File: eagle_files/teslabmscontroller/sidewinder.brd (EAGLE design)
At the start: 101.6 x 73.2 mm, 41 parts, among them J1 TERMINAL12, J2 TERMINAL12, Q1 2N3704, Q2 2N3906, T1 V_REG_317SINK, U1 G3VM41, U2 G3VM41, U3 G3VM41, U4 SN65HVD230, U5 SP720APP, U6 SP720APP

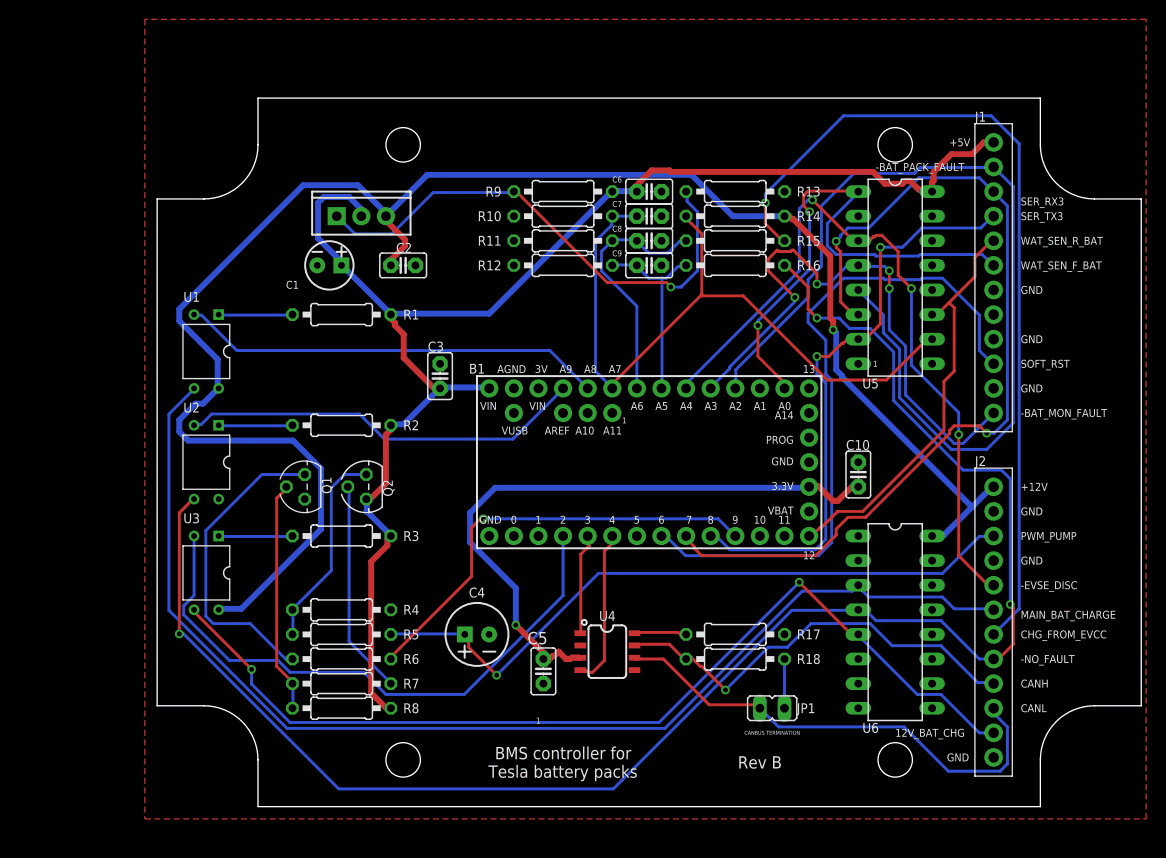
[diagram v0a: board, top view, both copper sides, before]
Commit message: fixed RUN
RUN signal was absent from connector
flipped whole board so silk alligns with OLED
fixed routing issu of can chip
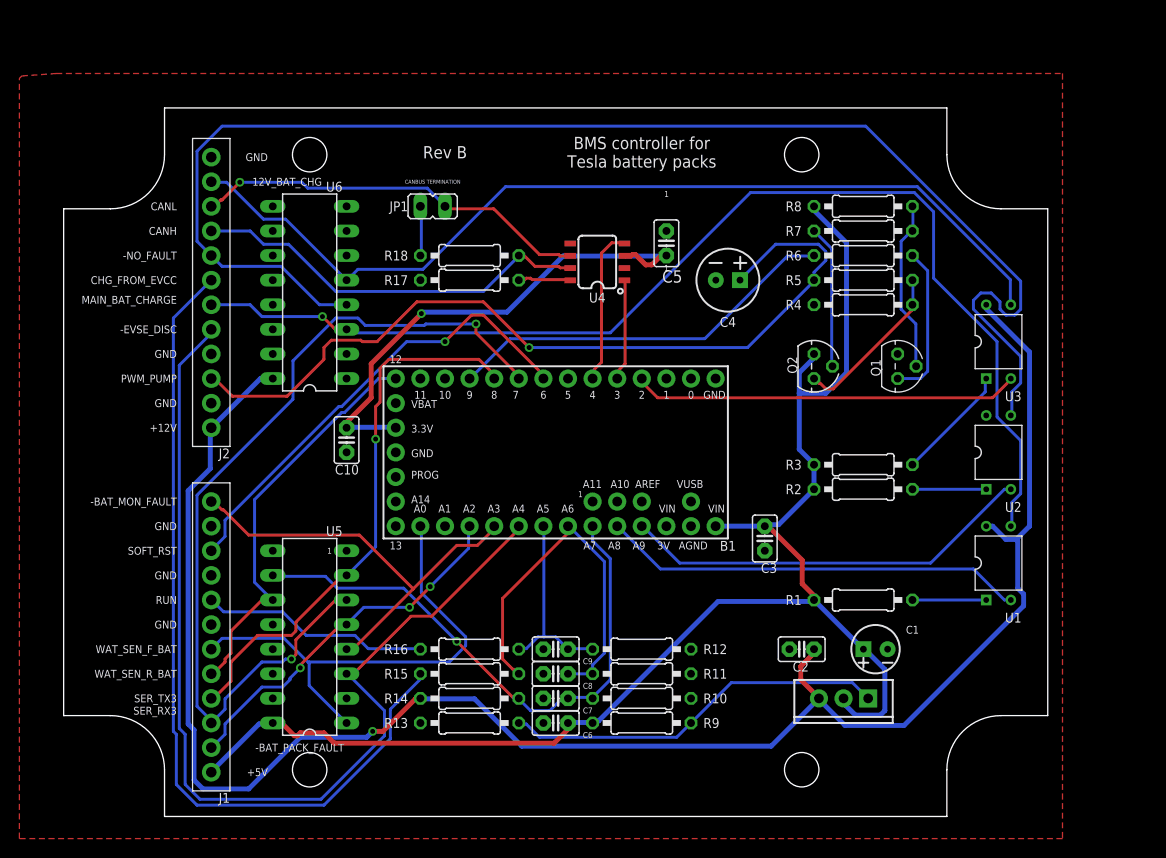
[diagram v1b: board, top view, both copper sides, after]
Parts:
- moved J2 94.3 mm to (3.05, 55.6), turned to 180 degrees
- moved J1 91.6 mm to (3.05, 20.1), turned to 180 degrees
- moved U3 85.2 mm to (86.9, 48.0), turned to 90 degrees
- moved U1 84.7 mm to (86.9, 25.1), turned to 90 degrees
- moved U2 81.8 mm to (86.9, 36.6), turned to 90 degrees
- moved R8 74.7 mm to (72.9, 62.0), turned to 180 degrees
- moved U5 72.3 mm to (15.7, 16.3), turned to 90 degrees
- moved R7 71.3 mm to (72.9, 59.4), turned to 180 degrees
- moved T1 70.4 mm to (70.9, 11.2), turned to 180 degrees
- moved C1 68.9 mm to (74.2, 16.3), turned to 180 degrees
- moved U6 68.2 mm to (15.7, 51.8), turned to 90 degrees
- moved R6 68.1 mm to (72.9, 56.9), turned to 0 degrees
- moved R5 65.1 mm to (72.9, 54.4), turned to 180 degrees
- moved JP1 62.6 mm to (28.4, 62.0), turned to 90 degrees
- moved Q1 62.5 mm to (76.5, 45.5), turned to 270 degrees
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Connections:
- net N$4 renamed PWM_PUMP
- new net RUN: J1.J8, R16.2
- net -NO_FAULT: no longer R16.2
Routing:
- net -BAT_PACK_FAULT: track 97.2 -> 38.4 mm, vias 0 -> 3
- net -EVSE_DISC: track 75.5 -> 104.9 mm, vias 3 -> 0
- net -NO_FAULT: track 171.8 -> 144.3 mm, vias 3 -> 0
- net RUN: track 0.00 -> 23.7 mm
- net SOFT_RST: track 70.2 -> 48.4 mm, vias 0 -> 1
- net -12V_BAT_CHG: track 61.5 -> 40.1 mm
- net PWM_PUMP: track 70.5 -> 86.9 mm
- net N$5: track 32.2 -> 16.0 mm
- net -BAT_MON_FAULT: track 60.2 -> 45.3 mm, vias 4 -> 0
- net 12VBAT_MON: track 73.4 -> 58.8 mm, vias 0 -> 1
- net N$15: track 53.3 -> 39.7 mm, vias 1 -> 0
- net CHARGING: track 26.1 -> 38.8 mm
- net +3V3: track 65.4 -> 53.2 mm
- net +12V: track 179.3 -> 190.3 mm
- net CANL: track 50.0 -> 41.3 mm, vias 0 -> 1
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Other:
- board text added: "RUN"

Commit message: bug fixes
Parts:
- added R19: 1k, rcl:0207/10
- moved R17 2.54 mm to (32.3, 51.8)
- moved R18 2.54 mm to (32.3, 54.4)
- moved C10 1.78 mm to (21.3, 37.8)
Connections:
- net -NO_FAULT: now also R19.1
- net CHARGING_FROM_EVCC: now also U6.12
- net RUN: now also R19.2, U6.15
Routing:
- net RUN: track 23.7 -> 75.8 mm, vias 0 -> 3
- net -NO_FAULT: track 144.3 -> 107.4 mm
- net CHARGING_FROM_EVCC: track 87.7 -> 53.7 mm, vias 0 -> 2
- net MAIN_BAT_CHARGE: track 119.3 -> 150.1 mm, vias 1 -> 0
- net SERIAL_TX3: track 57.1 -> 83.9 mm, vias 1 -> 3
- net +12V: track 190.3 -> 170.5 mm, vias 1 -> 3
- net -BAT_PACK_FAULT: track 38.4 -> 57.2 mm, vias 3 -> 1
- net PWM_PUMP: track 86.9 -> 73.0 mm, vias 1 -> 0
- net WAT_SEN_F_BAT: track 50.7 -> 41.1 mm
- net -EVSE_DISC: track 104.9 -> 96.4 mm, vias 0 -> 2
- net SOFT_RST: track 48.4 -> 54.2 mm
- net -BAT_MON_FAULT: track 45.3 -> 49.5 mm, vias 0 -> 1
- net 12VBAT_MON: track 58.8 -> 62.6 mm, vias 1 -> 0
- net N$13: track 5.16 -> 8.61 mm
- net CANH: track 41.8 -> 44.2 mm, vias 0 -> 1
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
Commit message: run and charging to zener
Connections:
- removed net N$2: B1.19, C9.1, R12.2, R16.1
- new net RUN_SW: J1.J8, R16.2
- net CHARGING: now also U5.9
- net RUN: now also B1.19, C9.1, R12.2, R16.1, U5.12; no longer J1.J8, R16.2
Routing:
- net RUN: track 75.8 -> 119.8 mm, vias 3 -> 0
- net CHARGING_FROM_EVCC: track 53.7 -> 93.1 mm, vias 2 -> 0
- net RUN_SW: track 0.00 -> 25.6 mm
- net CHARGING: track 38.8 -> 62.1 mm, vias 0 -> 2
- net WAT_SEN_R_BAT: track 40.1 -> 62.5 mm, vias 2 -> 0
- net MAIN_BAT_CHARGE: track 150.1 -> 127.9 mm, vias 0 -> 1
- net N$2: track 20.2 -> 0.00 mm
- net -BAT_PACK_FAULT: track 57.2 -> 40.3 mm, vias 1 -> 3
- net -EVSE_DISC: track 96.4 -> 112.7 mm, vias 2 -> 1
- net SERIAL_TX3: track 83.9 -> 68.2 mm, vias 3 -> 4
- net WAT_SEN_F_BAT: track 41.1 -> 52.4 mm
- net CANL: track 41.7 -> 50.2 mm
- net PWM_PUMP: track 73.0 -> 81.1 mm, vias 0 -> 2
- net +5V: track 152.7 -> 146.5 mm
- net N$13: track 8.61 -> 11.9 mm
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
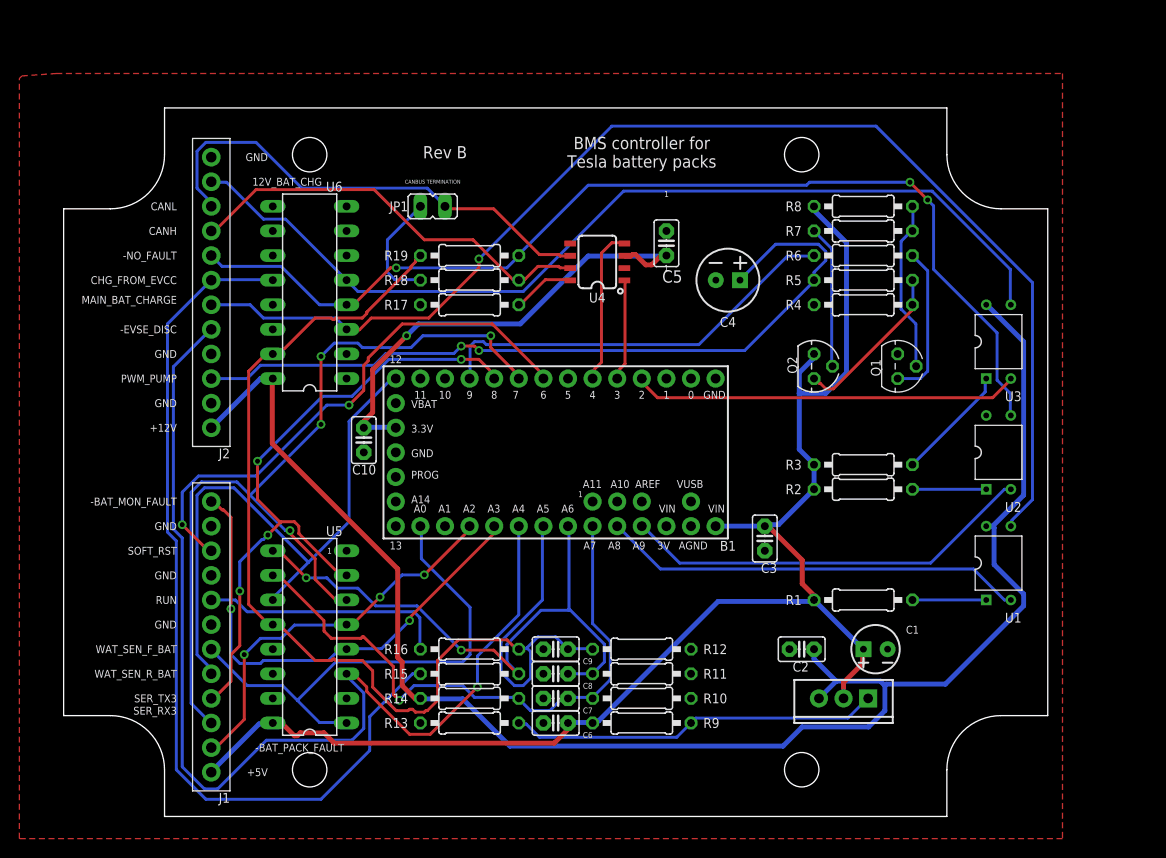
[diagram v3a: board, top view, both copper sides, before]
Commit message: adjusted 12Vto5V deviders
changed 2 resistors from 10k to 15k after we fried a board...
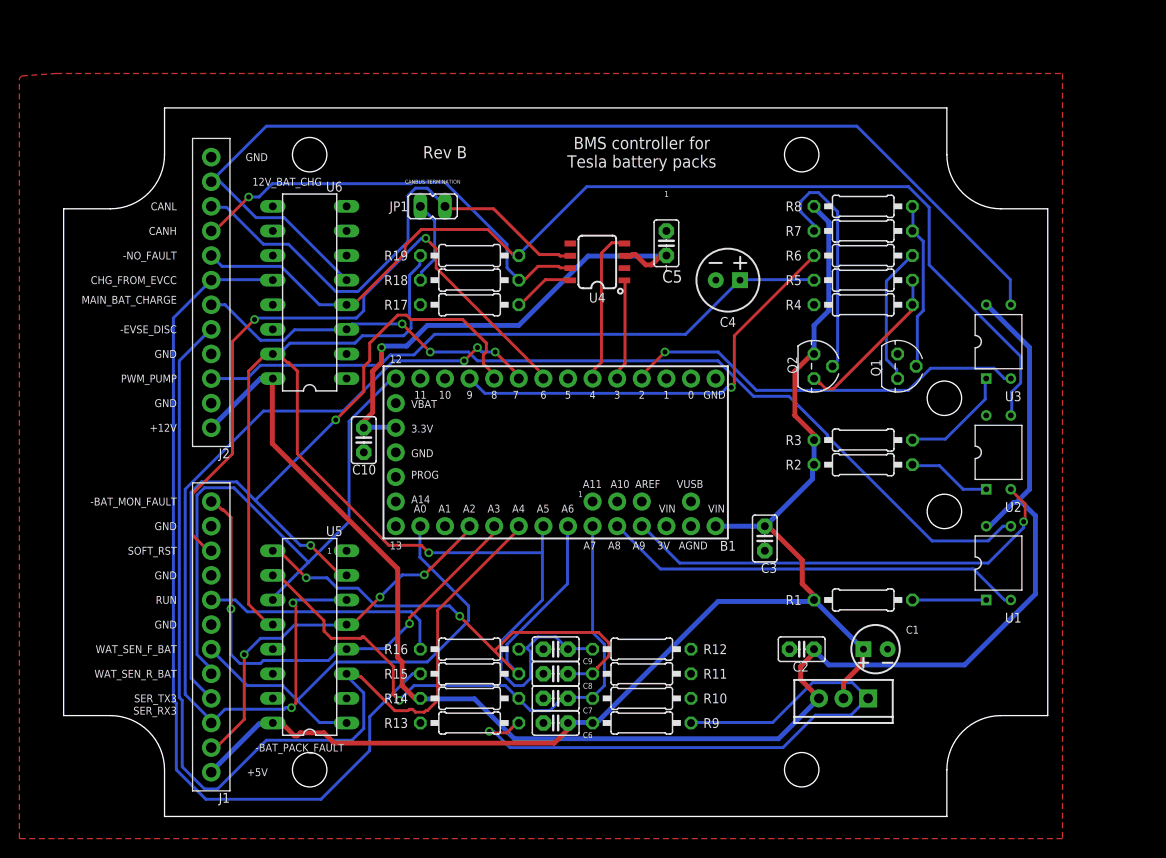
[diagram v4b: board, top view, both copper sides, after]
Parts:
- R15, R16: value 10k -> 15k
- moved R2 2.54 mm to (72.9, 35.3)
- moved R3 2.54 mm to (72.9, 37.8)
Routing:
- net MAIN_BAT_CHARGE: track 127.9 -> 94.8 mm, vias 1 -> 2
- net N$15: track 38.4 -> 66.2 mm, vias 0 -> 1
- net PWM_PUMP: track 81.1 -> 66.5 mm, vias 2 -> 0
- net SERIAL_TX3: track 68.2 -> 82.5 mm, vias 4 -> 2
- net 12V_BAT_CHG: track 98.5 -> 112.6 mm
- net SOFT_RST: track 56.2 -> 69.1 mm
- net N$7: track 14.8 -> 24.8 mm
- net RUN: track 119.8 -> 128.4 mm, vias 0 -> 1
- net +5V: track 146.5 -> 138.7 mm
- net CHARGING: track 62.1 -> 68.5 mm
- net +12V: track 168.1 -> 163.3 mm
- net N$1: track 42.8 -> 47.2 mm, vias 0 -> 1
- net -EVSE_DISC: track 112.7 -> 108.5 mm, vias 1 -> 0
- net SERIAL_RX3: track 89.4 -> 93.0 mm, vias 4 -> 5
- net N$13: track 11.9 -> 8.86 mm
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
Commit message: added EVCC_config.txt
added the config of the EVCC controller
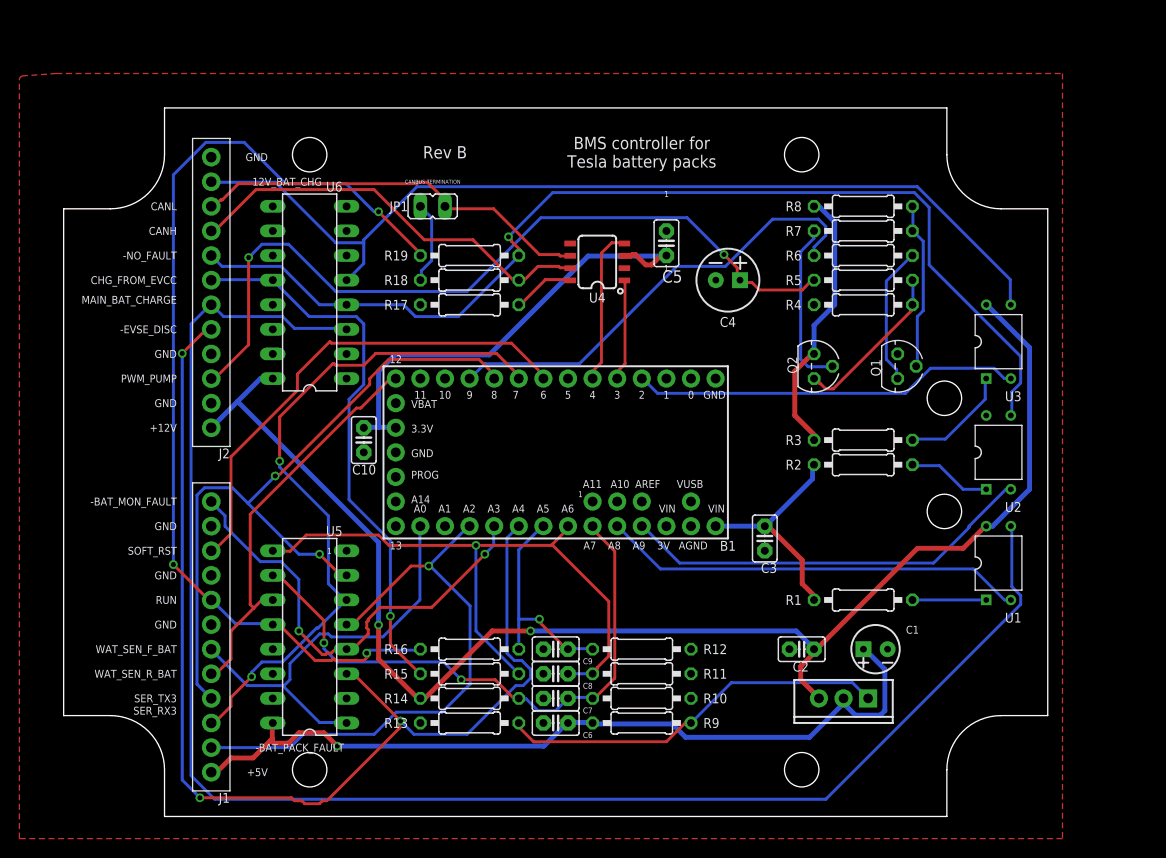
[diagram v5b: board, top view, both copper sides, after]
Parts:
- R15, R16: value 15k -> 20k
- R19: value 1k -> 20k
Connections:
- net +3V3: now also R1.1, R2.1, R3.1
- net +5V: now also R19.2; no longer R1.1, R2.1, R3.1
- net RUN: no longer R19.2, U5.12, U6.15
- net RUN_SW: now also U5.12
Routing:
- net RUN: track 128.4 -> 23.0 mm
- net RUN_SW: track 25.4 -> 102.6 mm, vias 0 -> 3
- net MAIN_BAT_CHARGE: track 94.8 -> 168.1 mm, vias 2 -> 0
- net CHARGING_FROM_EVCC: track 92.6 -> 57.5 mm, vias 0 -> 1
- net N$15: track 66.2 -> 40.3 mm, vias 1 -> 0
- net SERIAL_RX3: track 93.0 -> 70.7 mm, vias 5 -> 2
- net WAT_SEN_R_BAT: track 62.5 -> 41.9 mm
- net -BAT_PACK_FAULT: track 40.3 -> 60.4 mm, vias 3 -> 1
- net SOFT_RST: track 69.1 -> 50.7 mm, vias 2 -> 0
- net PWM_PUMP: track 66.5 -> 82.6 mm, vias 0 -> 2
- net +12V: track 163.3 -> 147.9 mm, vias 0 -> 2
- net 12V_BAT_CHG: track 112.6 -> 98.9 mm
- net CANL: track 50.9 -> 41.7 mm
- net -EVSE_DISC: track 108.5 -> 117.3 mm, vias 0 -> 3
- net SERIAL_TX3: track 82.5 -> 74.1 mm
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
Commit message: updated BMS board
fixed can bus chip and changed 5v regulator to a switching to avoid heat.
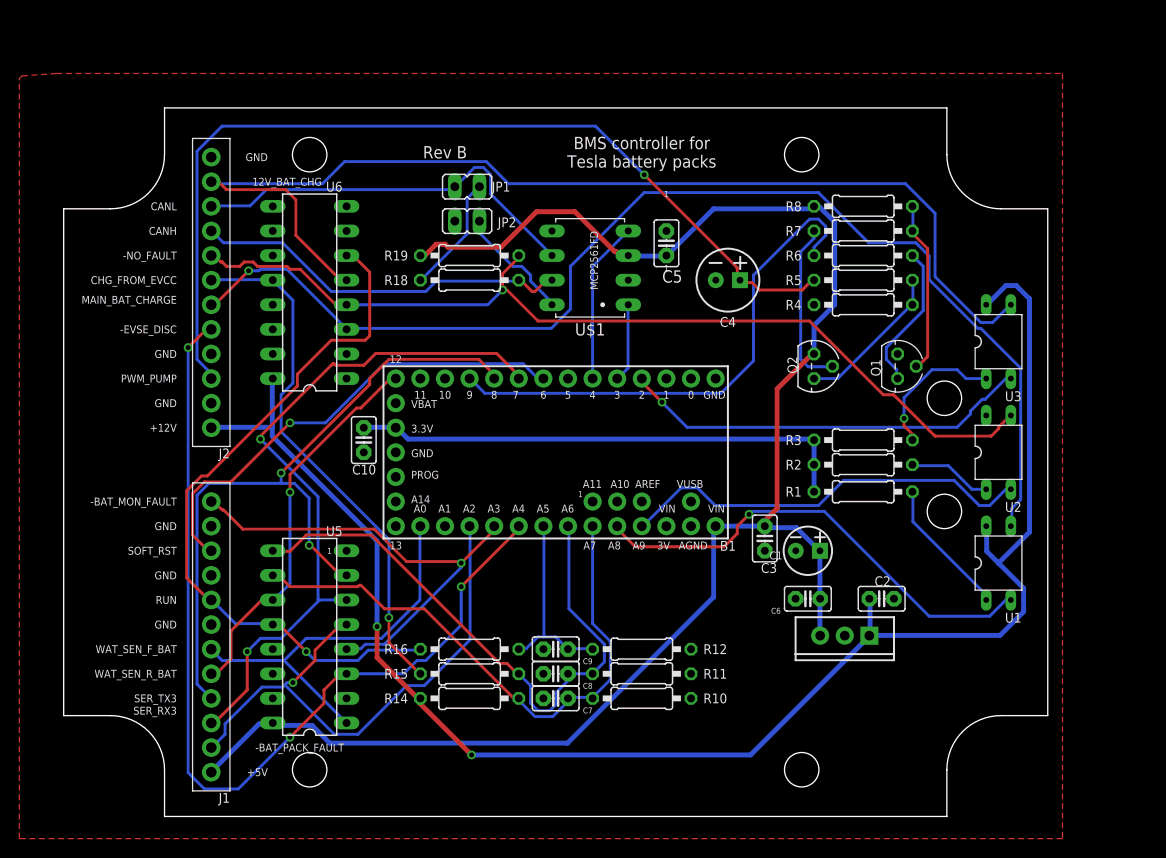
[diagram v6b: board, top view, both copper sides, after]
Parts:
- removed R13: 3k, rcl:0207/10
- removed R17: 10k, rcl:0207/10
- removed R9: 1k, rcl:0207/10
- removed T1: V_REG_317SINK, SparkFun-IC-Power:TO220-ADJ
- removed U4: SN65HVD230, SparkFun-Retired:SO08
- added JP2: STDBY, jumper:JP1
- added U$1: MCP2561FDDIP8, MCP2561FD:DIP787W45P254L949H533Q8B
- added U7: mEZD72401A-G, SparkFun-IC-Power:TO220-IGO
- JP1: value on -> BUS TERM
- moved C6 29.0 mm to (67.2, 21.5)
- moved C1 12.3 mm to (67.2, 26.4), turned to 0 degrees
- moved R1 11.2 mm to (72.9, 32.5)
- moved C2 9.76 mm to (74.8, 21.5), turned to 0 degrees
- moved JP1 4.10 mm to (32.0, 64.0), turned to 270 degrees
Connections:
- removed net N$15: R13.2, R9.1, T1.ADJ
- net +12V: now also U7.IN; no longer T1.IN
- net +3V3: no longer C5.1, U4.3
- net +5V: now also C5.1, U$1.3, U7.OUT; no longer R9.2, T1.OUT
- net CANH: now also U$1.7; no longer U4.7
- net CANL: now also U$1.6; no longer U4.6
- net CAN_RX: now also U$1.4; no longer U4.4
- net CAN_TX: now also U$1.1; no longer U4.1
- net GND: now also JP2.2, U$1.2, U7.GND; no longer R13.1, R17.2, U4.2
- net N$12: now also JP2.1, U$1.8; no longer R17.1, U4.8
- net RUN_SW: now also U6.6
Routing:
- net MAIN_BAT_CHARGE: track 168.1 -> 121.8 mm, vias 0 -> 1
- net N$15: track 40.3 -> 0.00 mm
- net +5V: track 137.0 -> 173.5 mm, vias 1 -> 0
- net RUN_SW: track 102.6 -> 73.1 mm, vias 3 -> 1
- net -EVSE_DISC: track 117.3 -> 96.4 mm
- net +12V: track 147.9 -> 165.9 mm
- net 12V_BAT_CHG: track 98.9 -> 115.4 mm
- net PWM_PUMP: track 82.6 -> 97.1 mm, vias 2 -> 1
- net -NO_FAULT: track 111.3 -> 97.2 mm
- net N$8: track 7.62 -> 14.4 mm
- net N$3: track 47.4 -> 53.9 mm
- net N$12: track 6.40 -> 12.3 mm
- net -EVCC_ON: track 43.8 -> 48.8 mm, vias 0 -> 1
- net CHARGING: track 66.7 -> 62.4 mm, vias 1 -> 0
- net CANH: track 43.4 -> 39.3 mm
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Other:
- board text removed: "CANBUS TERMINATION"

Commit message: fixed CAN
Fixed can bus
fixed bug on PCB where run input was connected to both 5v and 12v chips.
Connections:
- net RUN_SW: no longer U5.12
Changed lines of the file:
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@@
 <contactref element="R16" pad="2"/>
 <contactref element="J1" pad="J8"/>
-<contactref element="U5" pad="12"/>
 <contactref element="U6" pad="6"/>
 <wire x1="8.0772" y1="18.8976" x2="11.8872" y2="18.8976" width="0.3048" layer="16"/>
 <wire x1="5.6388" y1="21.336" x2="8.0772" y2="18.8976" width="0.3048" layer="16"/>
-<wire x1="11.8872" y1="18.8976" x2="11.938" y2="18.796" width="0.3048" layer="16"/>
 <wire x1="5.6388" y1="21.336" x2="5.588" y2="21.336" width="0.3048" layer="16"/>
 <wire x1="21.7932" y1="16.1544" x2="27.1272" y2="16.1544" width="0.3048" layer="16"/>
@@
 <wire x1="12.0396" y1="18.7452" x2="12.6492" y2="18.7452" width="0.3048" layer="1"/>
 <wire x1="27.1272" y1="16.1544" x2="27.178" y2="16.256" width="0.3048" layer="16"/>
-<wire x1="12.0396" y1="18.7452" x2="11.938" y2="18.796" width="0.3048" layer="1"/>
 <wire x1="20.2692" y1="56.8452" x2="19.6596" y2="56.8452" width="0.3048" layer="1"/>
 <wire x1="21.9456" y1="55.1688" x2="20.2692" y2="56.8452" width="0.3048" layer="1"/>
@@
 <wire x1="19.6596" y1="56.8452" x2="19.558" y2="56.896" width="0.3048" layer="1"/>
 <via x="15.3924" y="16.002" extent="1-16" drill="0.508"/>
+<wire x1="11.8872" y1="18.8976" x2="12.0396" y2="18.7452" width="0" layer="19" extent="1-16"/>
 </signal>
 </signals>
